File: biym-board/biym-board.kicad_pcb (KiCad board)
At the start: 2 copper layers, 50.8 x 34 mm, 31 parts, among them J1 HEADER_01X02_JST_SH_SMD_VERTI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, J2 HEADER_01X03_JST_ZH_SMD_VERTI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, J3 HEADER_01X04_JST_ZH_SMD_VERTI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, J4 HEADER_01X03_JST_ZH_SMD_VERTI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, J5 HEADER_01X03_JST_ZH_SMD_VERTI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, J6 HEADER_01X03_JST_ZH_SMD_VERTI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, Q1 MOSFET-N-CH-EN, Q2 MOSFET-P-CH-EN, U1 BOOST_5V_RP402N501F, U2 DRV8311H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

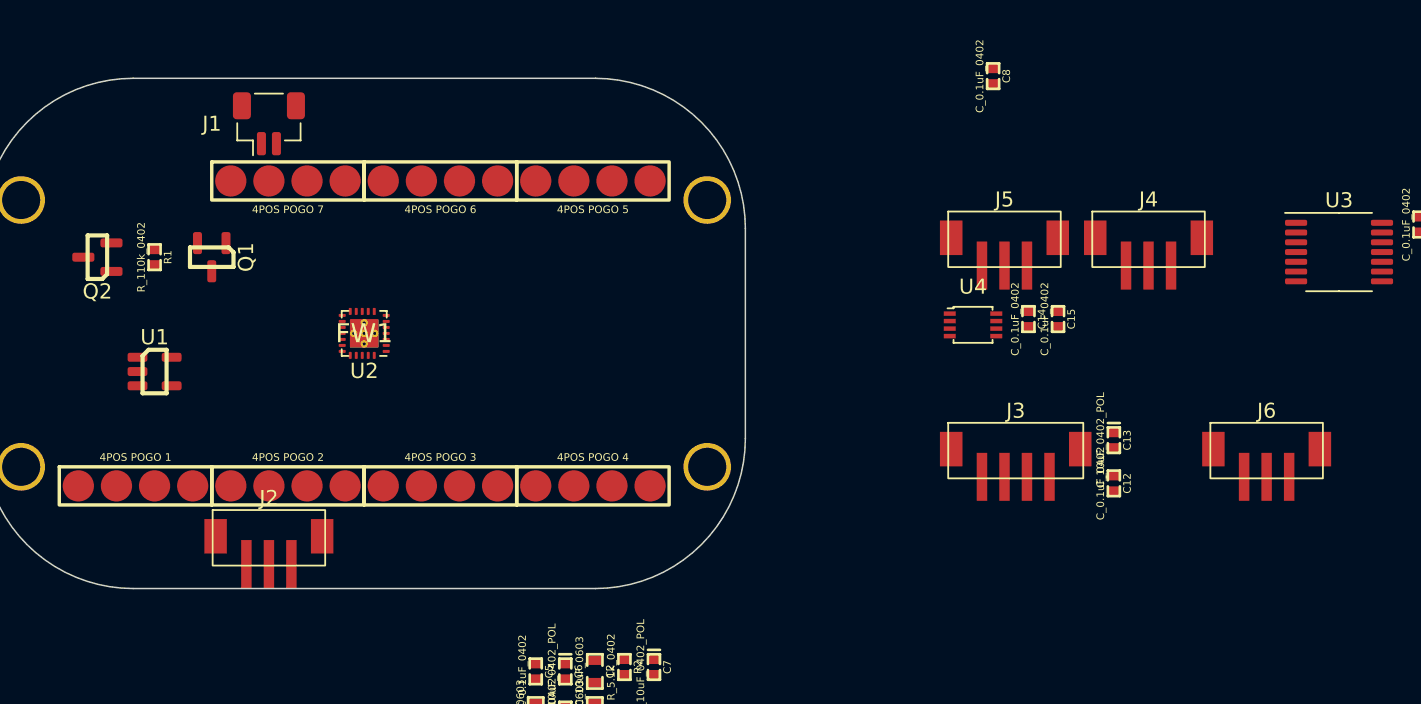
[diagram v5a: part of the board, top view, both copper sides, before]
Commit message: Check if there is room for connectors
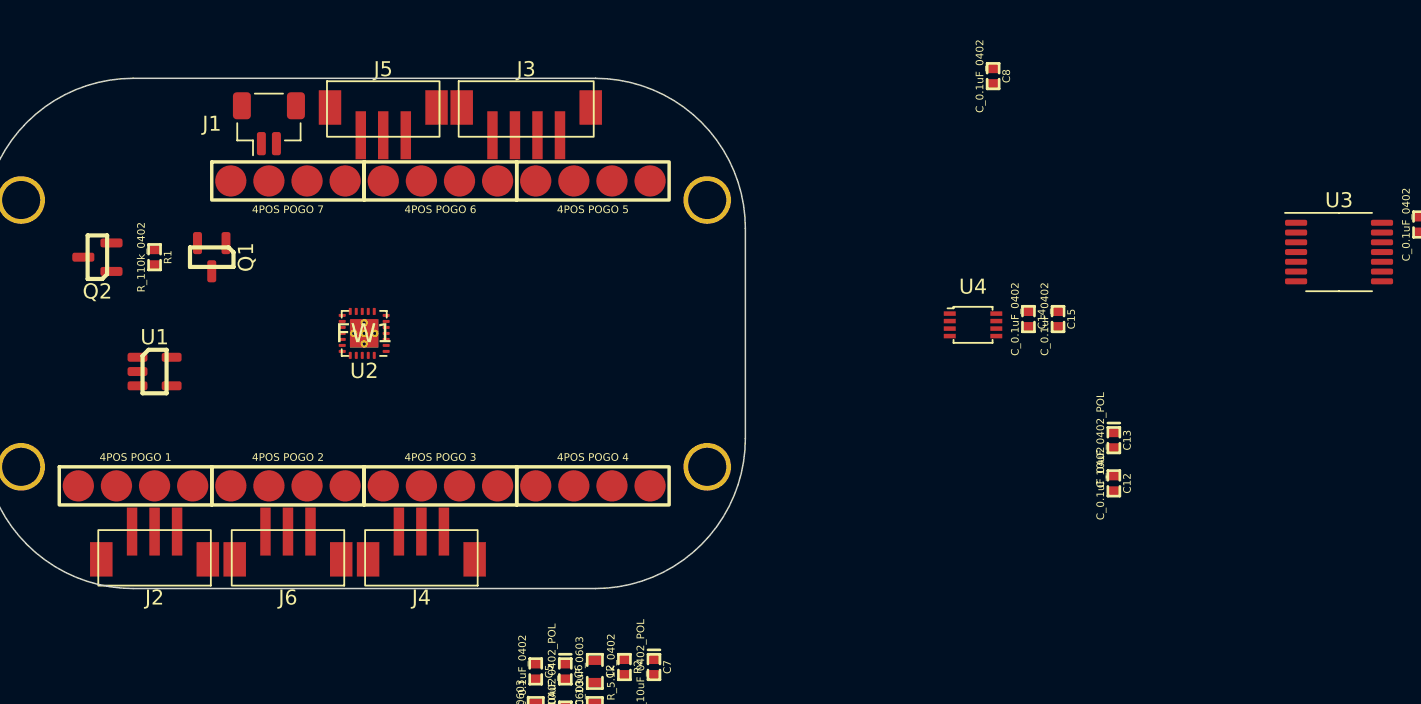
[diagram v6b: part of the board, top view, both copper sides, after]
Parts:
- moved J6 65.5 mm to (134.9, 114.6), turned to 180 degrees
- moved J4 52.6 mm to (143.8, 114.6), turned to 180 degrees
- moved J5 42.3 mm to (141.3, 85.4)
- moved J3 39.8 mm to (150.8, 85.4)
- moved J2 7.65 mm to (126.0, 114.6), turned to 180 degrees
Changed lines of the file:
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@@
   )
   (footprint "Janelia:JST_ZH_B3B_ZR_SM4_TF_1x03-1MP_P1.50mm_Vertical" (layer "F.Cu")
-    (at 182.6661 94.0781)
+    (at 141.27 85.395)
     (descr "JST ZE series connector, BM04B-ZESS-TBT (http://www.jst-mfg.com/product/pdf/eng/eZE.pdf), generated with kicad-footprint-generator")
     (tags "connector JST ZE vertical")
@@
   )
   (footprint "Janelia:JST_ZH_B3B_ZR_SM4_TF_1x03-1MP_P1.50mm_Vertical" (layer "F.Cu")
-    (at 133.65 113.97)
+    (at 126.03 114.605 180)
     (descr "JST ZE series connector, BM04B-ZESS-TBT (http://www.jst-mfg.com/product/pdf/eng/eZE.pdf), generated with kicad-footprint-generator")
     (tags "connector JST ZE vertical")
@@
     (fp_line (start 1.75 0.25) (end 1.75 -0.25) (layer "F.Fab") (width 0.1))
     (fp_line (start -1.25 0.25) (end -1.25 -0.25) (layer "F.Fab") (width 0.1))
-    (pad "1" smd rect (at -1.5 1.4) (size 0.7 3.2) (layers "F.Cu" "F.Paste" "F.Mask")
+    (pad "1" smd rect (at -1.5 1.4 180) (size 0.7 3.2) (layers "F.Cu" "F.Paste" "F.Mask")
       (net 34 "/driver/MOTOR_A") (pinfunction "Pin_1") (pintype "passive"))
-    (pad "2" smd rect (at 0 1.4) (size 0.7 3.2) (layers "F.Cu" "F.Paste" "F.Mask")
+    (pad "2" smd rect (at 0 1.4 180) (size 0.7 3.2) (layers "F.Cu" "F.Paste" "F.Mask")
       (net 35 "/driver/MOTOR_B") (pinfunction "Pin_2") (pintype "passive"))
-    (pad "3" smd rect (at 1.5 1.4) (size 0.7 3.2) (layers "F.Cu" "F.Paste" "F.Mask")
+    (pad "3" smd rect (at 1.5 1.4 180) (size 0.7 3.2) (layers "F.Cu" "F.Paste" "F.Mask")
       (net 36 "/driver/MOTOR_C") (pinfunction "Pin_3") (pintype "passive"))
-    (pad "MP" smd rect (at -3.55 -0.45) (size 1.5 2.3) (layers "F.Cu" "F.Paste" "F.Mask"))
-    (pad "MP" smd rect (at 3.55 -0.45) (size 1.5 2.3) (layers "F.Cu" "F.Paste" "F.Mask"))
+    (pad "MP" smd rect (at -3.55 -0.45 180) (size 1.5 2.3) (layers "F.Cu" "F.Paste" "F.Mask"))
+    (pad "MP" smd rect (at 3.55 -0.45 180) (size 1.5 2.3) (layers "F.Cu" "F.Paste" "F.Mask"))
     (model "${KICAD6_3DMODEL_DIR}/Connector_JST.3dshapes/JST_ZE_BM04B-ZESS-TBT_1x04-1MP_P1.50mm_Vertical.wrl"
       (offset (xyz 0 0 0))
@@
   )
   (footprint "Janelia:JST_ZH_B3B_ZR_SM4_TF_1x03-1MP_P1.50mm_Vertical" (layer "F.Cu")
-    (at 200.1361 108.1581)
+    (at 134.92 114.605 180)
     (descr "JST ZE series connector, BM04B-ZESS-TBT (http://www.jst-mfg.com/product/pdf/eng/eZE.pdf), generated with kicad-footprint-generator")
     (tags "connector JST ZE vertical")
@@
     (fp_line (start -0.25 -0.25) (end -0.25 0.25) (layer "F.Fab") (width 0.1))
     (fp_line (start 1.75 -0.25) (end 1.25 -0.25) (layer "F.Fab") (width 0.1))
-    (pad "1" smd rect (at -1.5 1.4) (size 0.7 3.2) (layers "F.Cu" "F.Paste" "F.Mask")
+    (pad "1" smd rect (at -1.5 1.4 180) (size 0.7 3.2) (layers "F.Cu" "F.Paste" "F.Mask")
       (net 4 "/GND") (pinfunction "Pin_1") (pintype "passive"))
-    (pad "2" smd rect (at 0 1.4) (size 0.7 3.2) (layers "F.Cu" "F.Paste" "F.Mask")
+    (pad "2" smd rect (at 0 1.4 180) (size 0.7 3.2) (layers "F.Cu" "F.Paste" "F.Mask")
       (net 8 "/GPIO_0") (pinfunction "Pin_2") (pintype "passive"))
-    (pad "3" smd rect (at 1.5 1.4) (size 0.7 3.2) (layers "F.Cu" "F.Paste" "F.Mask")
+    (pad "3" smd rect (at 1.5 1.4 180) (size 0.7 3.2) (layers "F.Cu" "F.Paste" "F.Mask")
       (net 9 "/GPIO_1") (pinfunction "Pin_3") (pintype "passive"))
-    (pad "MP" smd rect (at 3.55 -0.45) (size 1.5 2.3) (layers "F.Cu" "F.Paste" "F.Mask"))
-    (pad "MP" smd rect (at -3.55 -0.45) (size 1.5 2.3) (layers "F.Cu" "F.Paste" "F.Mask"))
+    (pad "MP" smd rect (at 3.55 -0.45 180) (size 1.5 2.3) (layers "F.Cu" "F.Paste" "F.Mask"))
+    (pad "MP" smd rect (at -3.55 -0.45 180) (size 1.5 2.3) (layers "F.Cu" "F.Paste" "F.Mask"))
     (model "${KICAD6_3DMODEL_DIR}/Connector_JST.3dshapes/JST_ZE_BM04B-ZESS-TBT_1x04-1MP_P1.50mm_Vertical.wrl"
       (offset (xyz 0 0 0))
@@
   )
   (footprint "Janelia:JST_ZH_B4B_ZR_SM4_TF_1x04-1MP_P1.50mm_Vertical" (layer "F.Cu")
-    (at 183.4161 108.1581)
+    (at 150.795 85.395)
     (descr "JST ZE series connector, BM04B-ZESS-TBT (http://www.jst-mfg.com/product/pdf/eng/eZE.pdf), generated with kicad-footprint-generator")
     (tags "connector JST ZE vertical")
@@
   )
   (footprint "Janelia:JST_ZH_B3B_ZR_SM4_TF_1x03-1MP_P1.50mm_Vertical" (layer "F.Cu")
-    (at 192.2661 94.0781)
+    (at 143.81 114.605 180)
     (descr "JST ZE series connector, BM04B-ZESS-TBT (http://www.jst-mfg.com/product/pdf/eng/eZE.pdf), generated with kicad-footprint-generator")
     (tags "connector JST ZE vertical")
@@
     (fp_line (start -1.25 0.25) (end -1.25 -0.25) (layer "F.Fab") (width 0.1))
     (fp_line (start -0.25 -0.25) (end -0.25 0.25) (layer "F.Fab") (width 0.1))
-    (pad "1" smd rect (at -1.5 1.4) (size 0.7 3.2) (layers "F.Cu" "F.Paste" "F.Mask")
+    (pad "1" smd rect (at -1.5 1.4 180) (size 0.7 3.2) (layers "F.Cu" "F.Paste" "F.Mask")
       (net 37 "/servo/TRANSLATED_SIGNAL_0") (pinfunction "Pin_1") (pintype "passive"))
-    (pad "2" smd rect (at 0 1.4) (size 0.7 3.2) (layers "F.Cu" "F.Paste" "F.Mask")
+    (pad "2" smd rect (at 0 1.4 180) (size 0.7 3.2) (layers "F.Cu" "F.Paste" "F.Mask")
       (net 3 "/VBOOSTED") (pinfunction "Pin_2") (pintype "passive"))
-    (pad "3" smd rect (at 1.5 1.4) (size 0.7 3.2) (layers "F.Cu" "F.Paste" "F.Mask")
+    (pad "3" smd rect (at 1.5 1.4 180) (size 0.7 3.2) (layers "F.Cu" "F.Paste" "F.Mask")
       (net 4 "/GND") (pinfunction "Pin_3") (pintype "passive"))
-    (pad "MP" smd rect (at 3.55 -0.45) (size 1.5 2.3) (layers "F.Cu" "F.Paste" "F.Mask"))
-    (pad "MP" smd rect (at -3.55 -0.45) (size 1.5 2.3) (layers "F.Cu" "F.Paste" "F.Mask"))
+    (pad "MP" smd rect (at 3.55 -0.45 180) (size 1.5 2.3) (layers "F.Cu" "F.Paste" "F.Mask"))
+    (pad "MP" smd rect (at -3.55 -0.45 180) (size 1.5 2.3) (layers "F.Cu" "F.Paste" "F.Mask"))
     (model "${KICAD6_3DMODEL_DIR}/Connector_JST.3dshapes/JST_ZE_BM04B-ZESS-TBT_1x04-1MP_P1.50mm_Vertical.wrl"
       (offset (xyz 0 0 0))

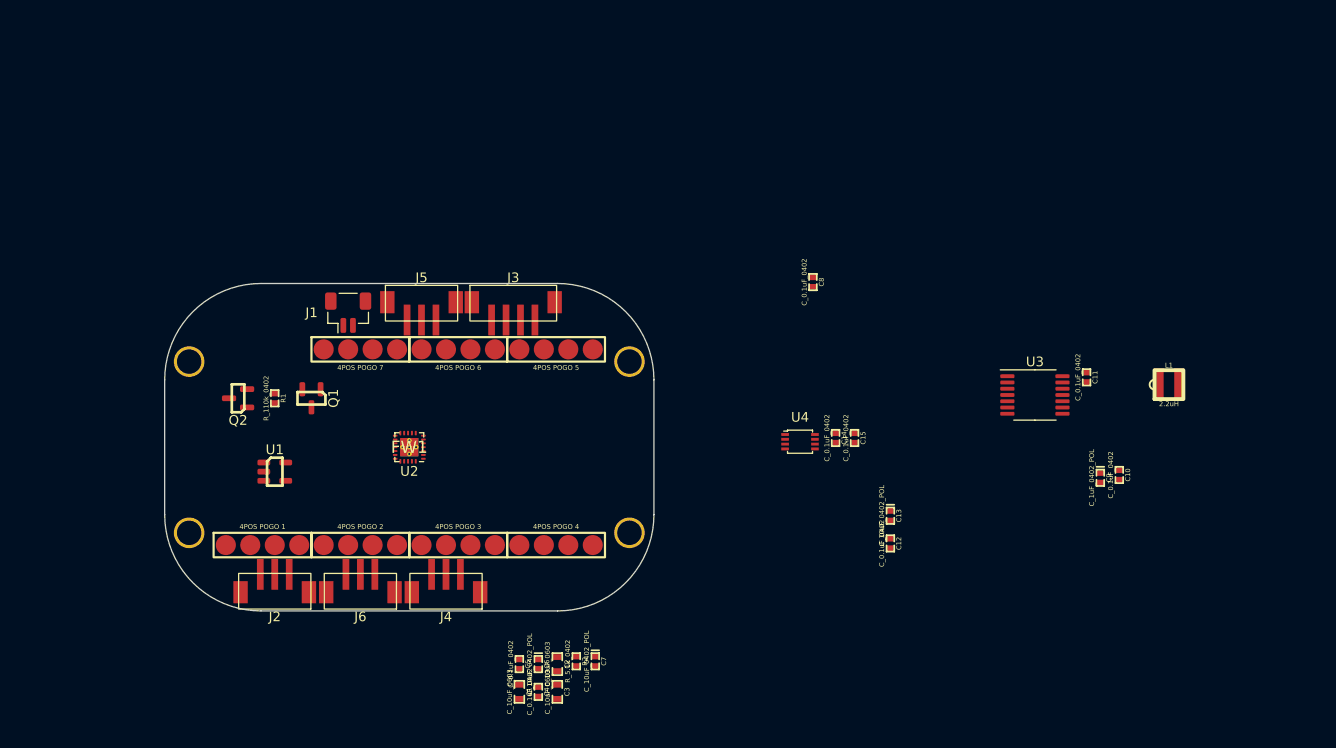
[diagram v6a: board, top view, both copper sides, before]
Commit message: Add boost for both led and servo
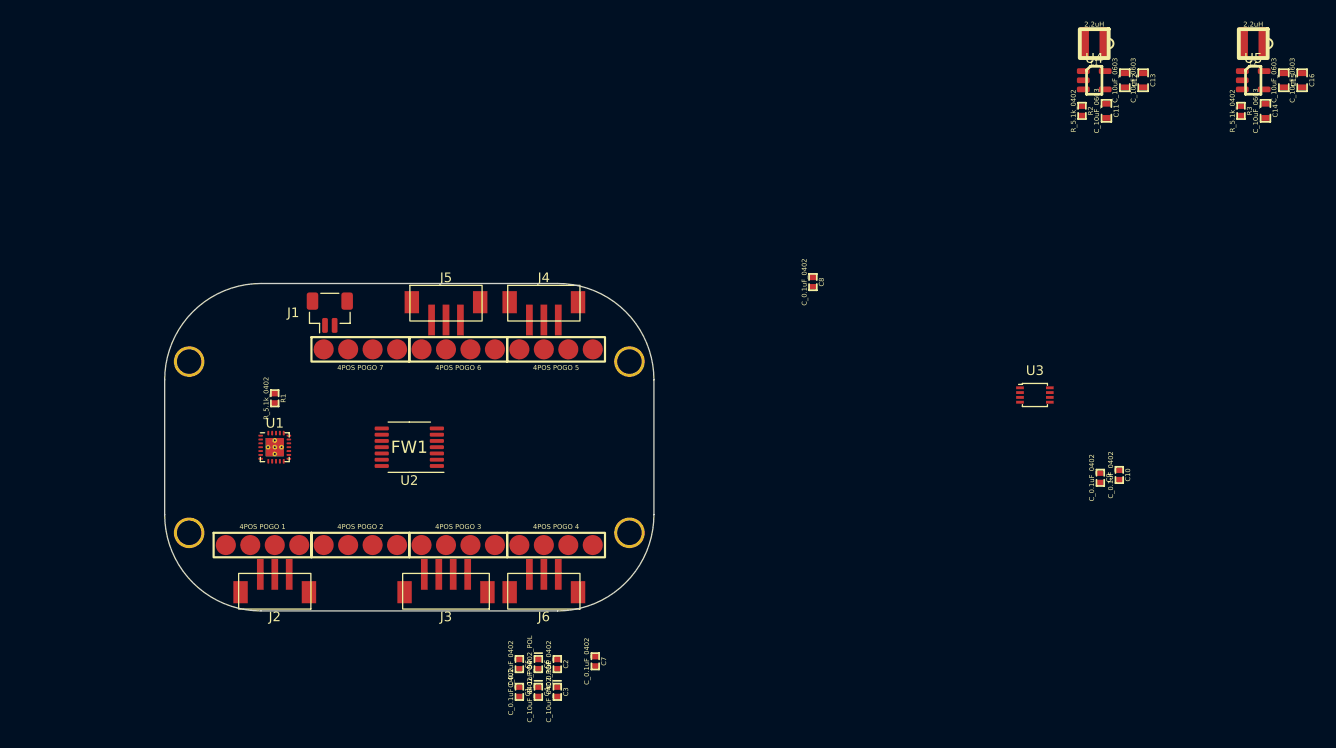
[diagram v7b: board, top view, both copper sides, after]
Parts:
- removed Q1: MOSFET-N-CH-EN, Janelia:SOT-23-3
- removed Q2: MOSFET-P-CH-EN, Janelia:SOT-23-3
- added C16: C_10uF_0603, Janelia:SM0603, F.Cu at (232.7, 61.9)
- added L2: 2.2uH, Janelia:INDUCTOR_VLS_HBX, F.Cu at (227.6, 58.1)
- added R3: R_5.1k_0402, Janelia:SM0402, F.Cu at (226.4, 65.1)
- added U5: BOOST_5V_RP402N501F, Janelia:SOT-23-5, F.Cu at (227.6, 61.9)
- C1, C2: value C_10uF_0603 -> C_0.1uF_0402; footprint Janelia:SM0603 -> Janelia:SM0402
- C11, C12, C14, C15: value C_0.1uF_0402 -> C_10uF_0603; footprint Janelia:SM0402 -> Janelia:SM0603
- C13: value C_10uF_0402_POL -> C_10uF_0603; footprint Janelia:SM0402_POL -> Janelia:SM0603
- C3: value C_10uF_0603 -> C_10uF_0402_POL; footprint Janelia:SM0603 -> Janelia:SM0402_POL
- C4: value C_0.1uF_0402 -> C_10uF_0402_POL; footprint Janelia:SM0402 -> Janelia:SM0402_POL
- C6: value C_10uF_0402_POL -> C_1uF_0402_POL
- C7: value C_10uF_0402_POL -> C_0.1uF_0402; footprint Janelia:SM0402_POL -> Janelia:SM0402
- C9: value C_1uF_0402_POL -> C_0.1uF_0402; footprint Janelia:SM0402_POL -> Janelia:SM0402
- R1: value R_110k_0402 -> R_5.1k_0402
- U1: value BOOST_5V_RP402N501F -> DRV8311H; footprint Janelia:SOT-23-5 -> Janelia:WQFN-24-1EP_3x3mm_P0.4mm_EP1.9x1.9mm_ThermalVias
- U2: value DRV8311H -> AS5047P; footprint Janelia:WQFN-24-1EP_3x3mm_P0.4mm_EP1.9x1.9mm_ThermalVias -> Janelia:TSSOP-14_4.4x5mm_P0.65mm
- U3: value AS5047P -> LT_SN74LVC2T45DCUT; footprint Janelia:TSSOP-14_4.4x5mm_P0.65mm -> Janelia:VSSOP-8_2.4x2.1mm_P0.5mm
- U4: value LT_SN74LVC2T45DCUT -> BOOST_5V_RP402N501F; footprint Janelia:VSSOP-8_2.4x2.1mm_P0.5mm -> Janelia:SOT-23-5
- moved R2 77.6 mm to (209.8, 65.1)
- moved C15 58.0 mm to (230.8, 61.9)
- moved C14 56.1 mm to (228.9, 65.1)
- moved C12 53.9 mm to (214.3, 61.9)
- moved C13 52.3 mm to (216.2, 61.9)
- moved U4 48.4 mm to (211.1, 61.9)
- moved L1 36.3 mm to (211.1, 58.1), turned to 180 degrees
- moved J4 30.9 mm to (154.0, 85.4), turned to 0 degrees
- moved J3 30.0 mm to (143.8, 114.6), turned to 180 degrees
- moved C11 27.7 mm to (212.4, 65.1)
- moved J6 19.1 mm to (154.0, 114.6)
- moved U1 2.54 mm to (126.0, 100.0)
- moved J5 2.54 mm to (143.8, 85.4)
- moved J1 1.91 mm to (131.7, 86.0)
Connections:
- C10 pad 1: /driver/CSAREF -> /VSERVO
- C11 pad 1: /VDIGITAL -> /VBATTERY
- C12 pad 1: /VPERIPHERAL -> /VLED
- C13 pad 1: /VPERIPHERAL -> /VLED
- C14 pad 1: /VDIGITAL -> /VBATTERY
- C15 pad 1: /VBOOSTED -> /VSERVO
- C2 pad 1: /VBOOSTED -> /VDIGITAL
- C3 pad 1: /VBOOSTED -> /VBATTERY
- C4 pad 1: /VPERIPHERAL -> /VDIGITAL
- C5 pad 1: /VDIGITAL -> /VBATTERY
- C5 pad 2: /GND -> /driver/CP
- C6 pad 1: /VPERIPHERAL -> /driver/VDD
- C7 pad 1: /VDIGITAL -> /driver/CSAREF
- C8 pad 1: /VPERIPHERAL -> /VDIGITAL
- C8 pad 2: /driver/CP -> /GND
- C9 pad 1: /driver/VDD -> /VDIGITAL
- FW1 pad 14: unconnected-(FW1-Pad14) -> /GPIO_1
- FW1 pad 15: unconnected-(FW1-Pad15) -> /GPIO_0
- FW1 pad 19: /GPIO_0 -> unconnected-(FW1-Pad19)
- FW1 pad 20: /GPIO_1 -> unconnected-(FW1-Pad20)
- FW1 pad 23: /DRIVER_PWM_A -> /DRIVER_PWM_C
- FW1 pad 25: /DRIVER_PWM_C -> /DRIVER_PWM_A
- FW1 pad 3: /ENABLE_PERIPHERAL_POWER -> /ENABLE_LED_POWER
- FW1 pad 7: /ENABLE_BOOSTED_POWER -> /ENABLE_SERVO_POWER
- J1 pad 1: /~{DISABLE_ALL_POWER} -> /GND
- J1 pad 2: /GND -> /~{DISABLE_ALL_POWER}
- J2 pad 1: /driver/MOTOR_A -> /driver/MOTOR_C
- J2 pad 3: /driver/MOTOR_C -> /driver/MOTOR_A
- J3 pad 4: /VPERIPHERAL -> /VLED
- J4 pad 2: /VBOOSTED -> /VSERVO
- J5 pad 2: /VBOOSTED -> /VSERVO
- J6 pad 1: /GND -> /GPIO_0
- J6 pad 2: /GPIO_0 -> /GND
- L1 pad 2: /power/LX -> /power/boost_led/LX
- R1 pad 1: /VBATTERY -> /VDIGITAL
- R1 pad 2: /power/~{ENABLE_PERIPHERAL} -> /~{DRIVER_FAULT}
- R2 pad 1: /VDIGITAL -> /ENABLE_LED_POWER
- R2 pad 2: /~{DRIVER_FAULT} -> /GND
- U1 pad 1: /power/LX -> /~{DRIVER_FAULT}
- U1 pad 2: /GND -> /driver/CSAREF
- U1 pad 3: /ENABLE_BOOSTED_POWER -> unconnected-(U1-Pad3)
- U1 pad 4: /VBATTERY -> unconnected-(U1-Pad4)
- U1 pad 5: /VBOOSTED -> unconnected-(U1-Pad5)
- U2 pad 1: /~{DRIVER_FAULT} -> /~{ENCODER_CS}
- U2 pad 10: /driver/MOTOR_A -> unconnected-(U2-Pad10)
- U2 pad 11: /driver/MOTOR_B -> /VDIGITAL
- U2 pad 12: /driver/MOTOR_C -> /VDIGITAL
- U2 pad 13: /DRIVER_PWM_C -> /GND
- U2 pad 14: /DRIVER_PWM_B -> unconnected-(U2-Pad14)
- U2 pad 2: /driver/CSAREF -> /SCK
- U2 pad 3: unconnected-(U2-Pad3) -> /MISO
- U2 pad 4: unconnected-(U2-Pad4) -> /MOSI
- U2 pad 5: unconnected-(U2-Pad5) -> /GND
- U2 pad 6: /driver/CP -> /ENCODER_B
- U2 pad 7: /VDIGITAL -> /ENCODER_A
- U2 pad 8: /VPERIPHERAL -> unconnected-(U2-Pad8)
- U2 pad 9: /GND -> unconnected-(U2-Pad9)
- U3 pad 1: /~{ENCODER_CS} -> /VDIGITAL
- U3 pad 2: /SCK -> /SERVO_SIGNAL_0
- U3 pad 3: /MISO -> /SERVO_SIGNAL_1
- U3 pad 4: /MOSI -> /GND
- U3 pad 5: /GND -> /VDIGITAL
- U3 pad 6: /ENCODER_B -> /servo/TRANSLATED_SIGNAL_1
- U3 pad 7: /ENCODER_A -> /servo/TRANSLATED_SIGNAL_0
- U3 pad 8: unconnected-(U3-Pad8) -> /VSERVO
- U4 pad 1: /VDIGITAL -> /power/boost_led/LX
- U4 pad 2: /SERVO_SIGNAL_0 -> /GND
- U4 pad 3: /SERVO_SIGNAL_1 -> /ENABLE_LED_POWER
- U4 pad 4: /GND -> /VBATTERY
- U4 pad 5: /VDIGITAL -> /VLED

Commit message: Initial footprint placement
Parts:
- J1: value HEADER_01X02_JST_SH_SMD_VERTICAL -> HEADER_01X02_JST_ZH_SMD_VERTICAL; footprint Janelia:JST_SH_BM02B-SRSS-TB_1x02-1MP_P1.00mm_Vertical -> Janelia:JST_ZH_B2B_ZR_SM4_TF_1x02-1MP_P1.50mm_Vertical
- moved L2 84.7 mm to (155.9, 103.2), turned to -90 degrees
- moved C16 81.5 mm to (159.7, 98.1), turned to 90 degrees
- moved C15 80.7 mm to (159.7, 100.0), turned to 90 degrees
- moved U5 79.5 mm to (159.7, 103.2), turned to 90 degrees
- moved C13 78.7 mm to (146.3, 98.1), turned to 180 degrees
- moved C14 75.6 mm to (162.9, 101.9), turned to 90 degrees
- moved C12 75.3 mm to (148.3, 98.1), turned to 180 degrees
- moved R3 74.7 mm to (162.9, 104.4), turned to 90 degrees
- moved L1 74.0 mm to (151.4, 101.9), turned to 0 degrees
- moved U4 69.8 mm to (151.4, 98.1), turned to 180 degrees
- moved C11 69.0 mm to (150.2, 94.9), turned to 180 degrees
- moved R2 64.5 mm to (152.7, 94.9), turned to 180 degrees
- moved C9 56.6 mm to (155.9, 94.3), turned to 180 degrees
- moved C10 54.7 mm to (159.7, 94.3), turned to 180 degrees
- moved C8 49.9 mm to (135.6, 101.3)
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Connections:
- FW1 pad 16: unconnected-(FW1-Pad16) -> /ENABLE_SERVO_POWER
- FW1 pad 17: unconnected-(FW1-Pad17) -> /SERVO_SIGNAL_0
- FW1 pad 18: unconnected-(FW1-Pad18) -> /SERVO_SIGNAL_1
- FW1 pad 19: unconnected-(FW1-Pad19) -> /ENCODER_B
- FW1 pad 20: unconnected-(FW1-Pad20) -> /ENCODER_A
- FW1 pad 21: /SERVO_SIGNAL_0 -> /DRIVER_PWM_C
- FW1 pad 22: /SERVO_SIGNAL_1 -> /DRIVER_PWM_B
- FW1 pad 23: /DRIVER_PWM_C -> /DRIVER_PWM_A
- FW1 pad 24: /DRIVER_PWM_B -> /~{DRIVER_SLEEP}
- FW1 pad 25: /DRIVER_PWM_A -> /~{DRIVER_FAULT}
- FW1 pad 5: /ENCODER_A -> unconnected-(FW1-Pad5)
- FW1 pad 6: /ENCODER_B -> unconnected-(FW1-Pad6)
- FW1 pad 7: /ENABLE_SERVO_POWER -> unconnected-(FW1-Pad7)
- FW1 pad 8: /~{DRIVER_FAULT} -> unconnected-(FW1-Pad8)
- FW1 pad 9: /~{DRIVER_SLEEP} -> unconnected-(FW1-Pad9)
